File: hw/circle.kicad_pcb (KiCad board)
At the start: 2 copper layers, 46 x 46 mm, 3 parts, among them U1 STM32F303CCTx

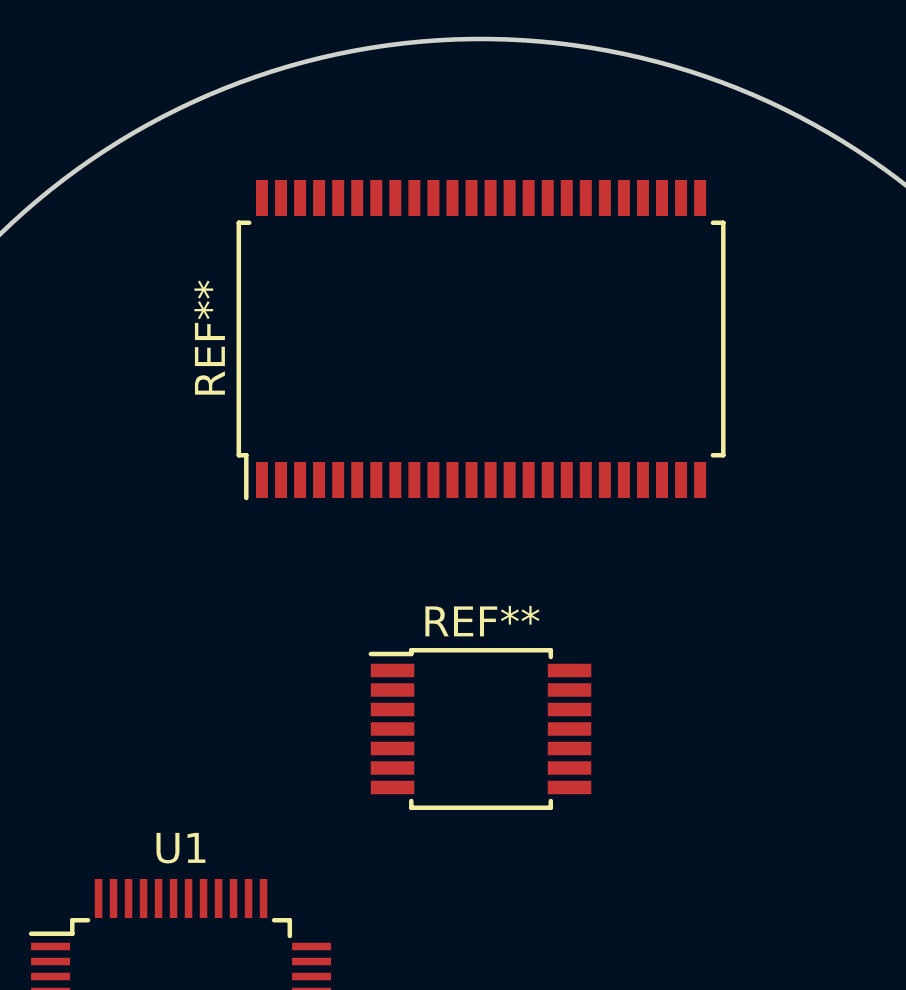
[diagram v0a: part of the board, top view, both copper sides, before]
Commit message: add encoder ic
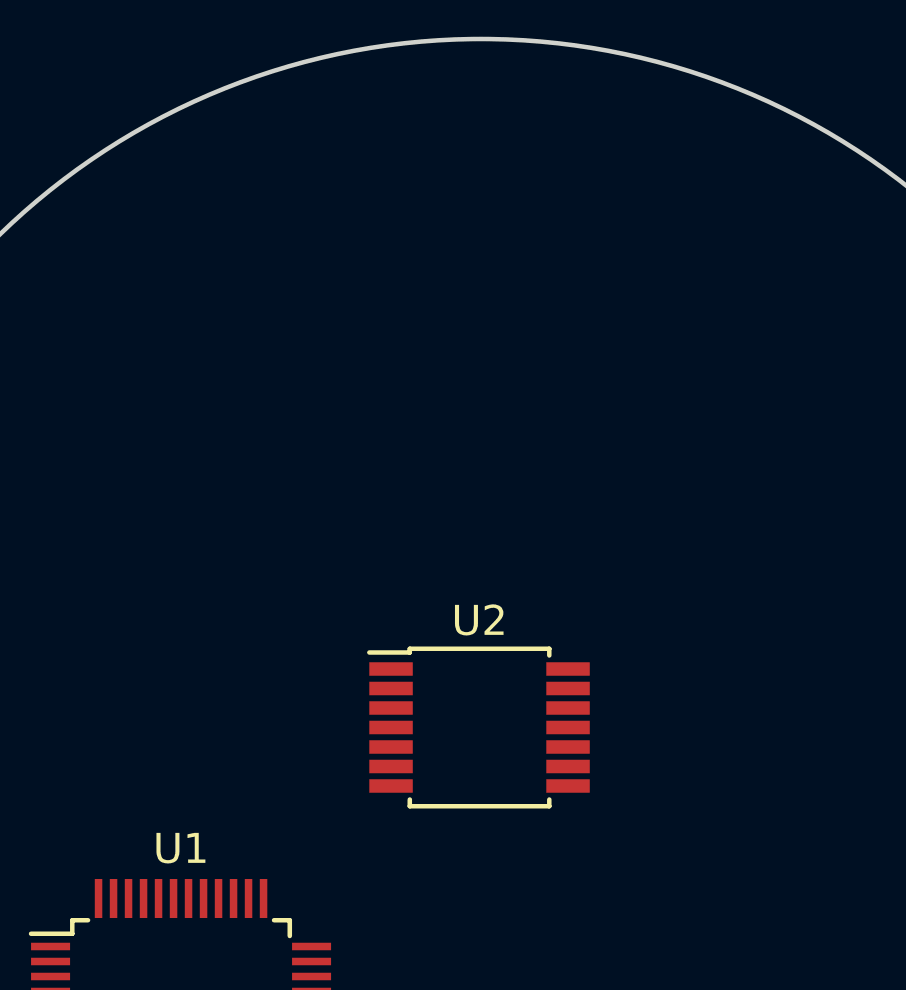
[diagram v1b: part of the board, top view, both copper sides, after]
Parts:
- removed REF**: SSOP-48_7.5x15.9mm_Pitch0.635mm, Housings_SSOP:SSOP-48_7.5x15.9mm_Pitch0.635mm
- removed REF**: TSSOP-14_4.4x5mm_Pitch0.65mm, Housings_SSOP:TSSOP-14_4.4x5mm_Pitch0.65mm
- added U2: AS5048A, Housings_SSOP:TSSOP-14_4.4x5mm_Pitch0.65mm, F.Cu at (100.0, 100.0)
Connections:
- U1 pad 23: Net-(U1-Pad23) -> GND
- U1 pad 35: Net-(U1-Pad35) -> GND
- U1 pad 36: Net-(U1-Pad36) -> +3V3
- U1 pad 47: Net-(U1-Pad47) -> GND
- U1 pad 8: Net-(U1-Pad8) -> GND

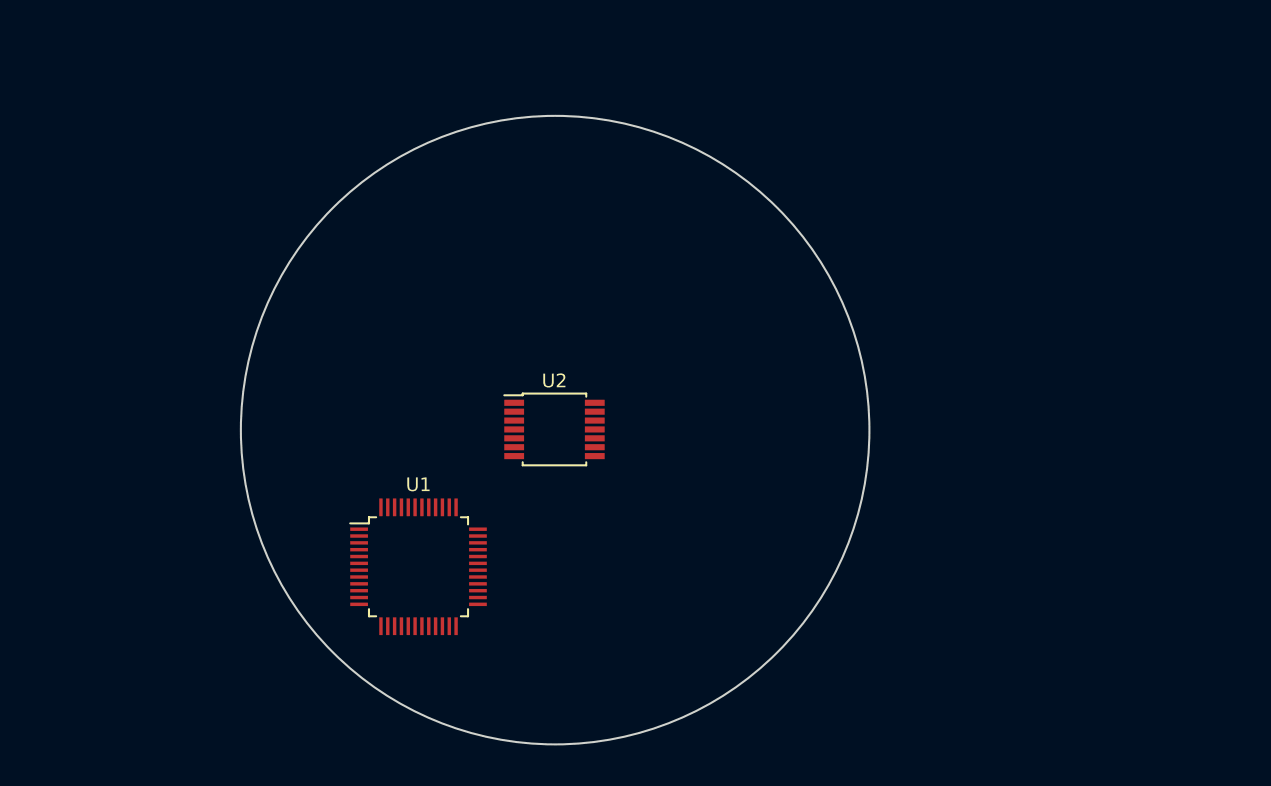
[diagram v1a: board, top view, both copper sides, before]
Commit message: filling in the schematic
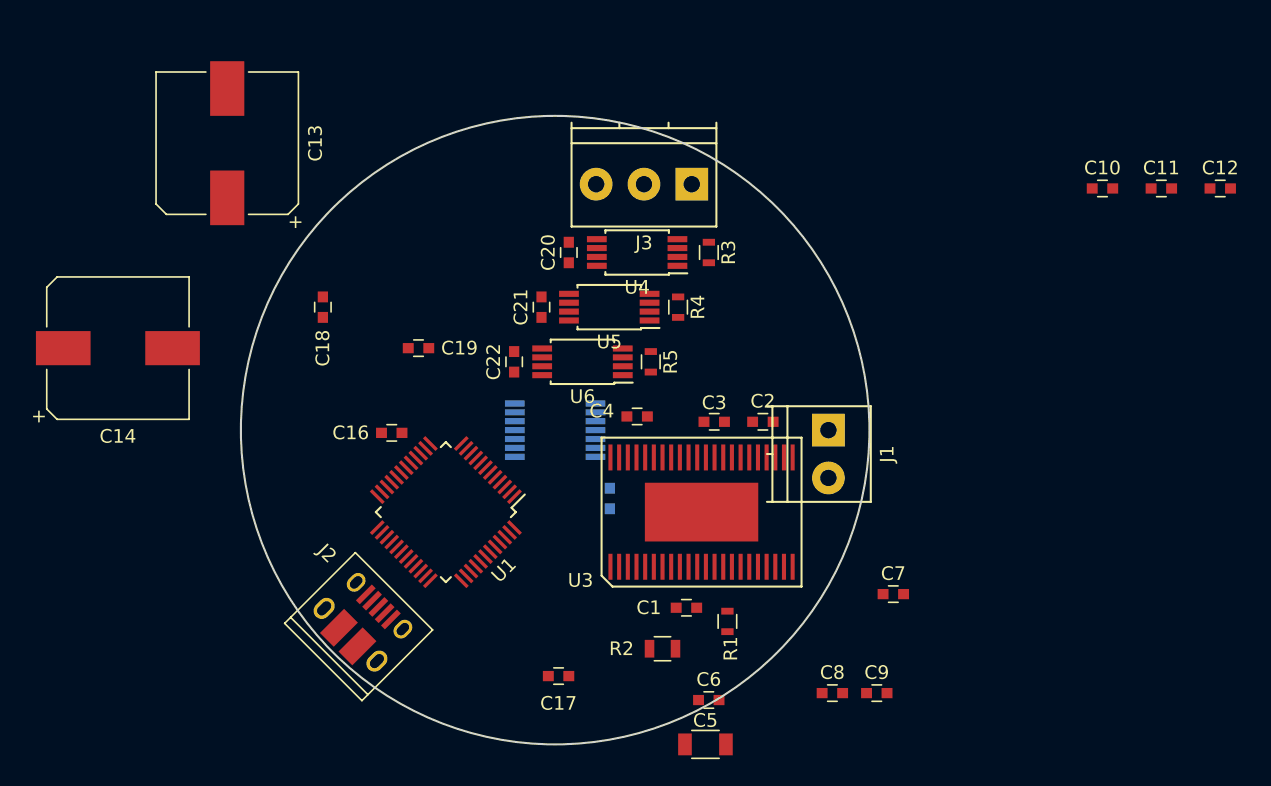
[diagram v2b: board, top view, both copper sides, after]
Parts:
- added C1: 100n, Capacitors_SMD:C_0603, F.Cu at (109.6, 113.0)
- added C10: 100n, Capacitors_SMD:C_0603, F.Cu at (140.1, 82.3)
- added C11: 100n, Capacitors_SMD:C_0603, F.Cu at (144.4, 82.3)
- added C12: 100n, Capacitors_SMD:C_0603, F.Cu at (148.7, 82.3)
- added C13: 1000u, Capacitors_SMD:CP_Elec_10x10.5, F.Cu at (76.0, 79.0)
- added C14: 1000u, Capacitors_SMD:CP_Elec_10x10.5, F.Cu at (68.0, 94.0)
- added C15: 100n, Capacitors_SMD:C_0603, B.Cu at (104.0, 105.0)
- added C16: 100n, Capacitors_SMD:C_0603, F.Cu at (88.0, 100.2)
- added C17: 100n, Capacitors_SMD:C_0603, F.Cu at (100.2, 118.0)
- added C18: 100n, Capacitors_SMD:C_0603, F.Cu at (83.0, 91.0)
- added C19: 100n, Capacitors_SMD:C_0603, F.Cu at (90.0, 94.0)
- added C2: 100n, Capacitors_SMD:C_0603, F.Cu at (115.2, 99.4)
- added C20: 100n, Capacitors_SMD:C_0603, F.Cu at (101.0, 87.0)
- added C21: 100n, Capacitors_SMD:C_0603, F.Cu at (99.0, 91.0)
- added C22: 100n, Capacitors_SMD:C_0603, F.Cu at (97.0, 95.0)
- added C3: 100n, Capacitors_SMD:C_0603, F.Cu at (111.6, 99.4)
- added C4: 100n, Capacitors_SMD:C_0603, F.Cu at (106.0, 99.0)
- added C5: 22u, Capacitors_SMD:C_1206, F.Cu at (111.0, 123.0)
- added C6: 100n, Capacitors_SMD:C_0603, F.Cu at (111.2, 119.8)
- added C7: 1u, Capacitors_SMD:C_0603, F.Cu at (124.8, 112.0)
- added C8: 1u, Capacitors_SMD:C_0603, F.Cu at (120.3, 119.2)
- added C9: 1u, Capacitors_SMD:C_0603, F.Cu at (123.5, 119.2)
- added J1: CONN_01X02, Terminal_Blocks:TerminalBlock_Pheonix_PT-3.5mm_2pol, F.Cu at (120.0, 100.0)
- added J2: USB_OTG, Connect:USB_Micro-B_10103594-0001LF, F.Cu at (86.0, 114.0)
- added J3: CONN_01X03, Terminal_Blocks:TerminalBlock_Pheonix_PT-3.5mm_3pol, F.Cu at (110.0, 82.0)
- added R1: 27k0, Resistors_SMD:R_0603, F.Cu at (112.6, 114.0)
- added R2: 1, Resistors_SMD:R_0805, F.Cu at (107.9, 116.0)
- added R3: 0R05, Resistors_SMD:R_0603, F.Cu at (111.2, 87.0)
- added R4: 0R05, Resistors_SMD:R_0603, F.Cu at (109.0, 91.0)
- added R5: 0R05, Resistors_SMD:R_0603, F.Cu at (107.0, 95.0)
- added U3: DRV8312, bldc:SOIC-44-POWERPAD, F.Cu at (110.7, 106.0)
- added U4: INA240, Housings_SSOP:TSSOP-8_4.4x3mm_Pitch0.65mm, F.Cu at (106.0, 87.0)
- added U5: INA240, Housings_SSOP:TSSOP-8_4.4x3mm_Pitch0.65mm, F.Cu at (104.0, 91.0)
- added U6: INA240, Housings_SSOP:TSSOP-8_4.4x3mm_Pitch0.65mm, F.Cu at (102.0, 95.0)
- U2: moved to B.Cu
- moved U1 4.47 mm to (92.0, 106.0), turned to 225 degrees
- moved U2 0.07 mm to (100.0, 100.0)
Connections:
- net Net-(U2-Pad1) renamed /ENC_CS
- net Net-(U2-Pad2) renamed /ENC_SCLK
- net Net-(U2-Pad3) renamed /ENC_MISO
- net Net-(U2-Pad4) renamed /ENC_MOSI
- U1 pad 32: Net-(U1-Pad32) -> /USBD-
- U1 pad 33: Net-(U1-Pad33) -> /USBD+
- U2 pad 11: Net-(U2-Pad11) -> +3V3
- U2 pad 12: Net-(U2-Pad11) -> +3V3

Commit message: rs485 transceiver
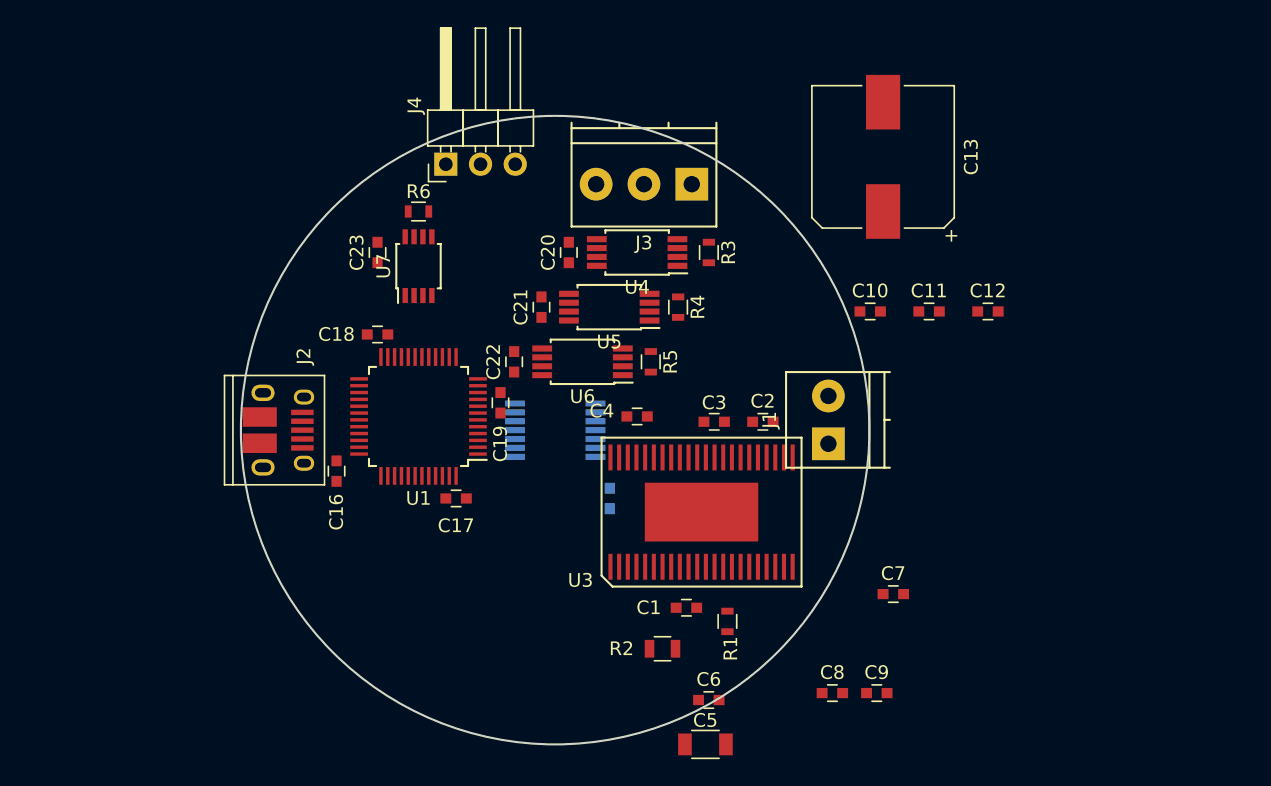
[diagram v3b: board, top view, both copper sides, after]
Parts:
- removed C14: 1000u, Capacitors_SMD:CP_Elec_10x10.5
- added C23: 100n, Capacitors_SMD:C_0603, F.Cu at (87.0, 87.0)
- added J4: CONN_01X03, Pin_Headers:Pin_Header_Angled_1x03_Pitch2.54mm, F.Cu at (92.0, 80.5)
- added R6: 100, Resistors_SMD:R_0603, F.Cu at (90.0, 84.0)
- added U7: SN65HVD75, Housings_SSOP:TSSOP-8_3x3mm_Pitch0.65mm, F.Cu at (90.0, 88.0)
- C13: value 1000u -> 470u
- moved C13 48.0 mm to (124.0, 80.0)
- moved C10 19.2 mm to (123.1, 91.3)
- moved C11 19.2 mm to (127.4, 91.3)
- moved C12 19.2 mm to (131.7, 91.3)
- moved J2 15.2 mm to (80.0, 100.0), turned to 270 degrees
- moved C17 15.0 mm to (92.8, 105.0)
- moved U1 7.28 mm to (90.0, 99.0), turned to 180 degrees
- moved C19 7.21 mm to (96.0, 98.0), turned to 90 degrees
- moved C16 4.92 mm to (84.0, 103.0), turned to 270 degrees
- moved C18 4.47 mm to (87.0, 93.0), turned to 180 degrees
- moved J1 1.00 mm to (120.0, 101.0), turned to 90 degrees

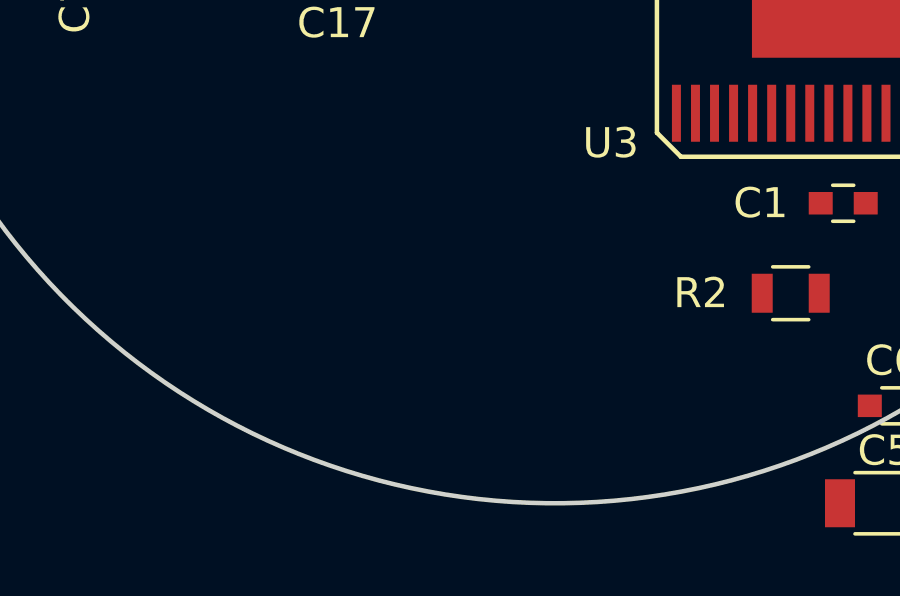
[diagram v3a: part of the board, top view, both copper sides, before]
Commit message: add r-78 dc/dc supply
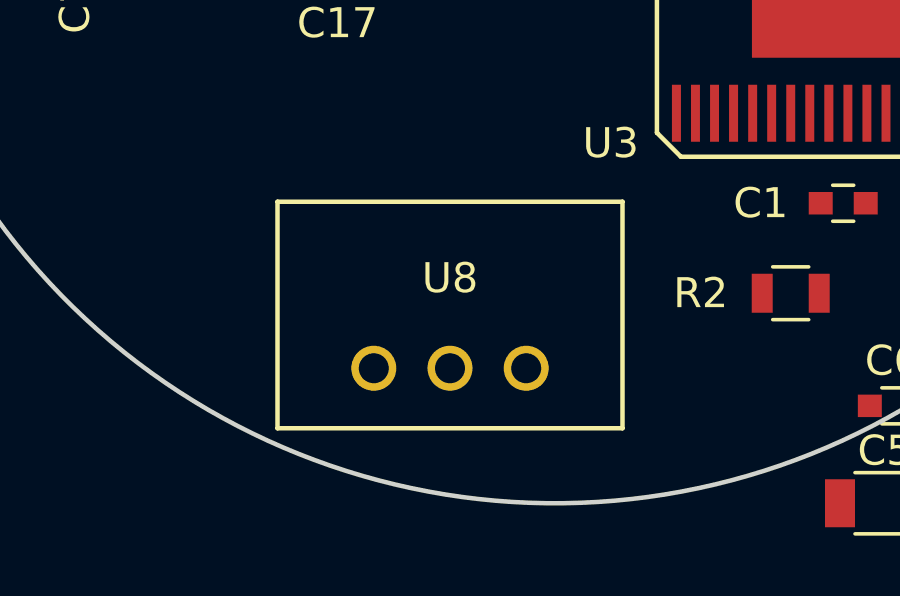
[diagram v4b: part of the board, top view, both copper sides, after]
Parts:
- added U8: R-78xx-0.5, DCDC:R-78xx-0.5, F.Cu at (96.5, 118.5)
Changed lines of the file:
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@@
 (kicad_pcb (version 20170123) (host pcbnew no-vcs-found-f007601~58~ubuntu16.04.1)
   (general
-    (links 125)
-    (no_connects 125)
+    (links 128)
+    (no_connects 128)
     (area 72.8725 69.914999 133.832339 126.0925)
     (thickness 1.6)
@@
     (tracks 0)
     (zones 0)
-    (modules 39)
+    (modules 40)
     (nets 90)
   )
@@
     (add_net VAA)
   )
+  (module DCDC:R-78xx-0.5 (layer F.Cu)
+    (at 96.5 118.5)
+    (fp_text reference U8 (at 0 -3) (layer F.SilkS)
+      (effects (font (size 1 1) (thickness 0.15)))
+    )
+    (fp_text value R-78xx-0.5 (at 0 -2.54) (layer F.Fab)
+      (effects (font (size 1 1) (thickness 0.15)))
+    )
+    (fp_line (start -5.75 2) (end -5.75 -5.55) (layer F.SilkS) (width 0.15))
+    (fp_line (start -5.75 2) (end 5.75 2) (layer F.SilkS) (width 0.15))
+    (fp_line (start -5.75 -5.55) (end 5.75 -5.55) (layer F.SilkS) (width 0.15))
+    (fp_line (start 5.75 -5.55) (end 5.75 2) (layer F.SilkS) (width 0.15))
+    (pad 3 thru_hole circle (at 2.54 0) (size 1.5 1.5) (drill 1) (layers *.Cu *.Mask)
+      (net 1 +3V3))
+    (pad 2 thru_hole circle (at 0 0) (size 1.5 1.5) (drill 1) (layers *.Cu *.Mask)
+      (net 42 GND))
+    (pad 1 thru_hole circle (at -2.54 0) (size 1.5 1.5) (drill 1) (layers *.Cu *.Mask)
+      (net 47 +12V))
+  )
   (module Pin_Headers:Pin_Header_Angled_1x03_Pitch2.54mm (layer F.Cu)

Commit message: rs485 connector
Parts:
- removed J4: CONN_01X03, Pin_Headers:Pin_Header_Angled_1x03_Pitch2.54mm
- added C14: 1u, Capacitors_SMD:C_0603, F.Cu at (99.0, 87.0)
- added J5: CONN_01X03, Pin_Headers:Pin_Header_Angled_1x03_Pitch2.54mm, F.Cu at (83.5, 112.0)
- added J6: CONN_01X06, Pin_Headers:Pin_Header_Straight_1x06_Pitch2.54mm, F.Cu at (81.7, 90.3)
- added L1: ferrite, Resistors_SMD:R_0603, F.Cu at (96.2, 92.5)
- moved C23 5.10 mm to (92.0, 86.0)
- moved R6 4.53 mm to (94.5, 83.5)
- moved U7 4.53 mm to (94.5, 87.5)
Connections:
- net Net-(U1-Pad34) renamed /SWDIO
- net Net-(U1-Pad37) renamed /SWCLK
- net Net-(U1-Pad5) renamed /OSC_IN
- net Net-(U1-Pad6) renamed /OSC_OUT
- net Net-(U1-Pad7) renamed /NRST
- U1 pad 1: Net-(U1-Pad1) -> +3V3
- U1 pad 44: Net-(U1-Pad44) -> GND

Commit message: swd, etc.
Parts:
- added C24: 12p, Capacitors_SMD:C_0603, F.Cu at (99.0, 106.5)
- added C25: 12p, Capacitors_SMD:C_0603, F.Cu at (100.0, 98.5)
- added C26: 100n, Capacitors_SMD:C_0603, F.Cu at (91.2, 110.5)
- added J4: CONN_02X05, Pin_Headers:Pin_Header_Straight_2x05_Pitch1.27mm, F.Cu at (80.3, 107.7)
- added X1: 8 MHz, Crystals:Crystal_SMD_5032-2pin_5.0x3.2mm, F.Cu at (99.0, 102.5)
- moved J5 11.6 mm to (72.0, 113.5)
- moved U8 1.80 mm to (98.0, 119.5)

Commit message: capacitors
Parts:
- added C27: 100u, Capacitors_SMD:CP_Elec_5x5.8, F.Cu at (91.0, 116.5)
- added C28: 220u, Capacitors_SMD:CP_Elec_6.3x7.7, F.Cu at (135.8, 101.2)
- C13: value 470u -> 220u; footprint Capacitors_SMD:CP_Elec_10x10.5 -> Capacitors_SMD:CP_Elec_6.3x7.7
- moved C13 12.9 mm to (116.5, 90.5), turned to 120 degrees
- moved U8 3.61 mm to (100.0, 116.5), turned to 180 degrees
